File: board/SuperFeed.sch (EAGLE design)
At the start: 15 parts

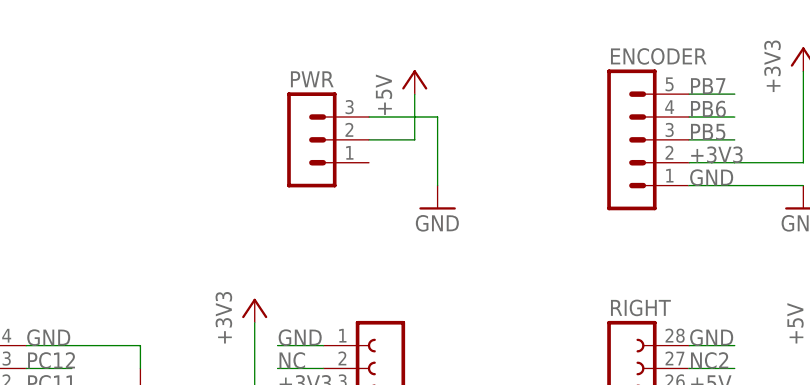
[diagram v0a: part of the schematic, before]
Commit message: Connect third pin to ground on power connector
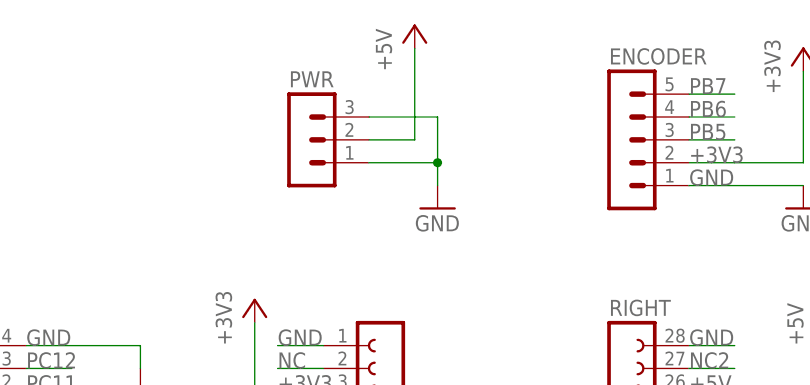
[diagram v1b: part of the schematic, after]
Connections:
- net GND: now also PWR.1
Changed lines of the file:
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@@
 <setting verticaltext="up"/>
 </settings>
-<grid distance="0.1" unitdist="inch" unit="inch" style="lines" multiple="1" display="yes" altdistance="0.01" altunitdist="inch" altunit="inch"/>
+<grid distance="0.1" unitdist="inch" unit="inch" style="lines" multiple="1" display="no" altdistance="0.01" altunitdist="inch" altunit="inch"/>
 <layers>
 <layer number="1" name="Top" color="4" fill="1" visible="no" active="no"/>
@@
 <instance part="PWR" gate="G$1" x="40.64" y="119.38"/>
 <instance part="SPINDLE" gate="1" x="88.9" y="-5.08"/>
-<instance part="P+4" gate="1" x="53.34" y="127"/>
+<instance part="P+4" gate="1" x="53.34" y="132.08"/>
 <instance part="GND4" gate="1" x="55.88" y="111.76"/>
 <instance part="GND5" gate="1" x="22.86" y="91.44"/>
@@
 <pinref part="PWR" gate="G$1" pin="3"/>
 <wire x1="48.26" y1="121.92" x2="55.88" y2="121.92" width="0.1524" layer="91"/>
-<wire x1="55.88" y1="121.92" x2="55.88" y2="114.3" width="0.1524" layer="91"/>
+<wire x1="55.88" y1="121.92" x2="55.88" y2="116.84" width="0.1524" layer="91"/>
 <pinref part="GND4" gate="1" pin="GND"/>
+<pinref part="PWR" gate="G$1" pin="1"/>
+<wire x1="55.88" y1="116.84" x2="55.88" y2="114.3" width="0.1524" layer="91"/>
+<wire x1="48.26" y1="116.84" x2="55.88" y2="116.84" width="0.1524" layer="91"/>
+<junction x="55.88" y="116.84"/>
 </segment>
 <segment>
@@
 <pinref part="P+4" gate="1" pin="+5V"/>
 <wire x1="48.26" y1="119.38" x2="53.34" y2="119.38" width="0.1524" layer="91"/>
-<wire x1="53.34" y1="119.38" x2="53.34" y2="124.46" width="0.1524" layer="91"/>
-</segment>
-<segment>
+<wire x1="53.34" y1="119.38" x2="53.34" y2="129.54" width="0.1524" layer="91"/>
+</segment>
+<segment>

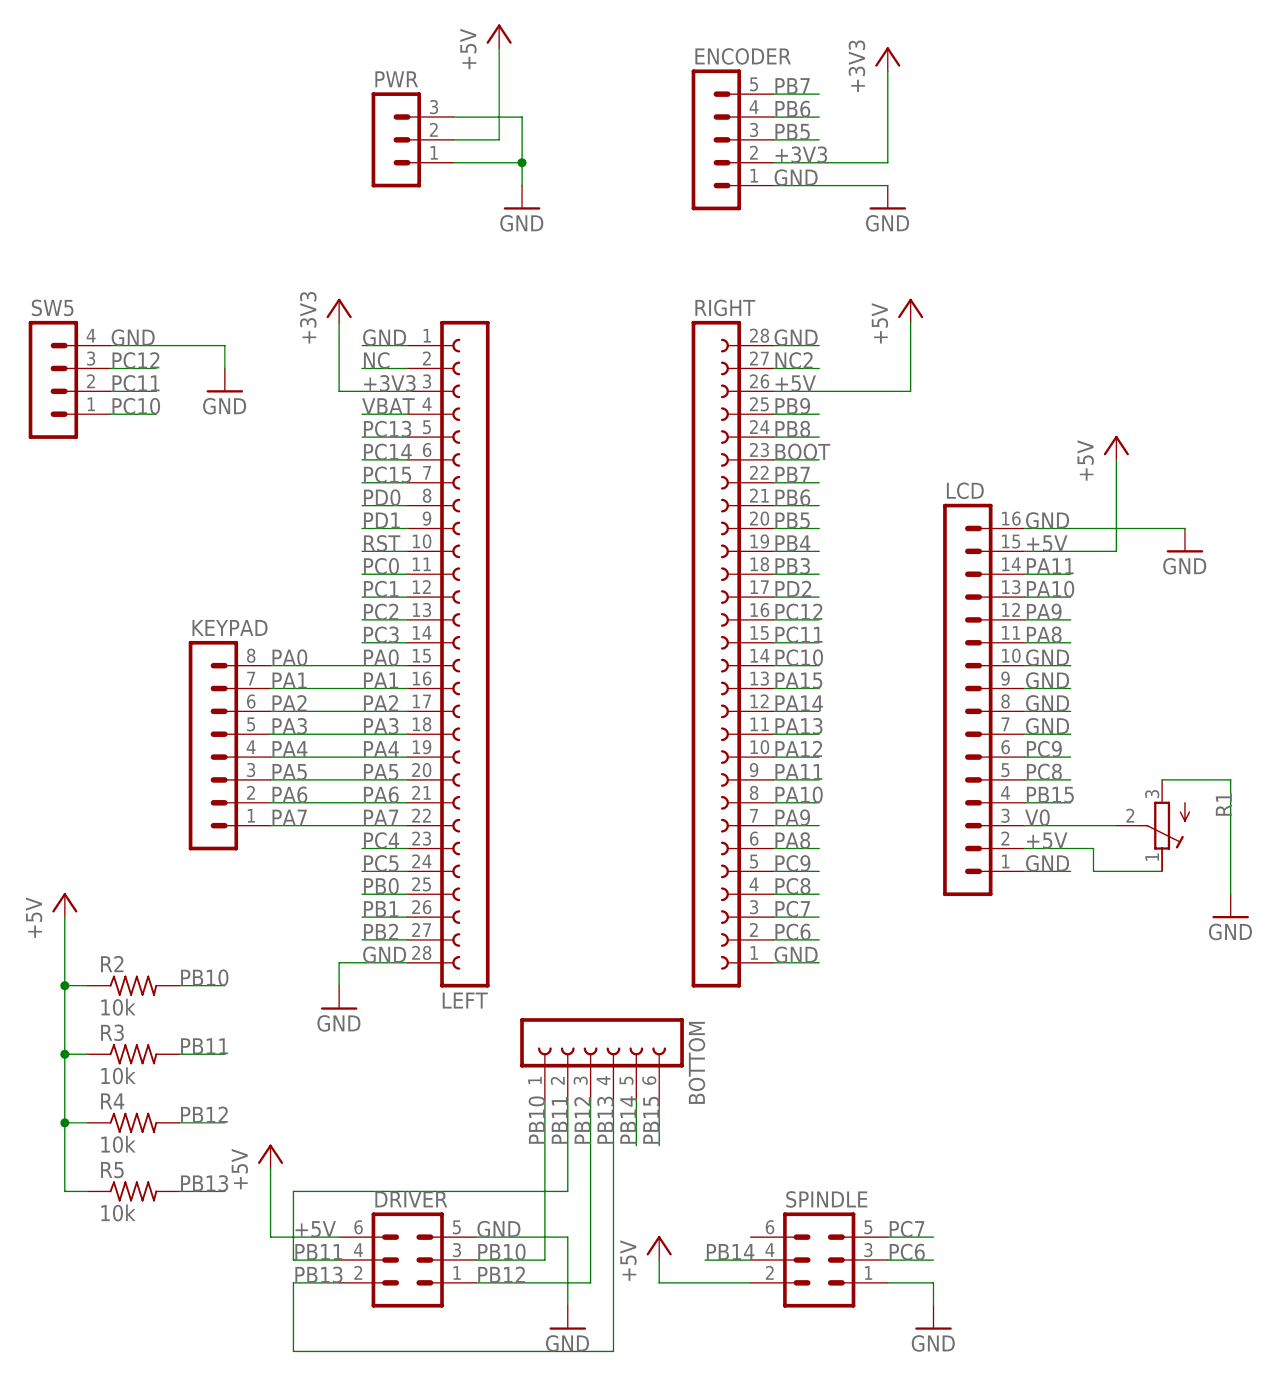
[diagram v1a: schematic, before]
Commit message: Adding extra buttons on board
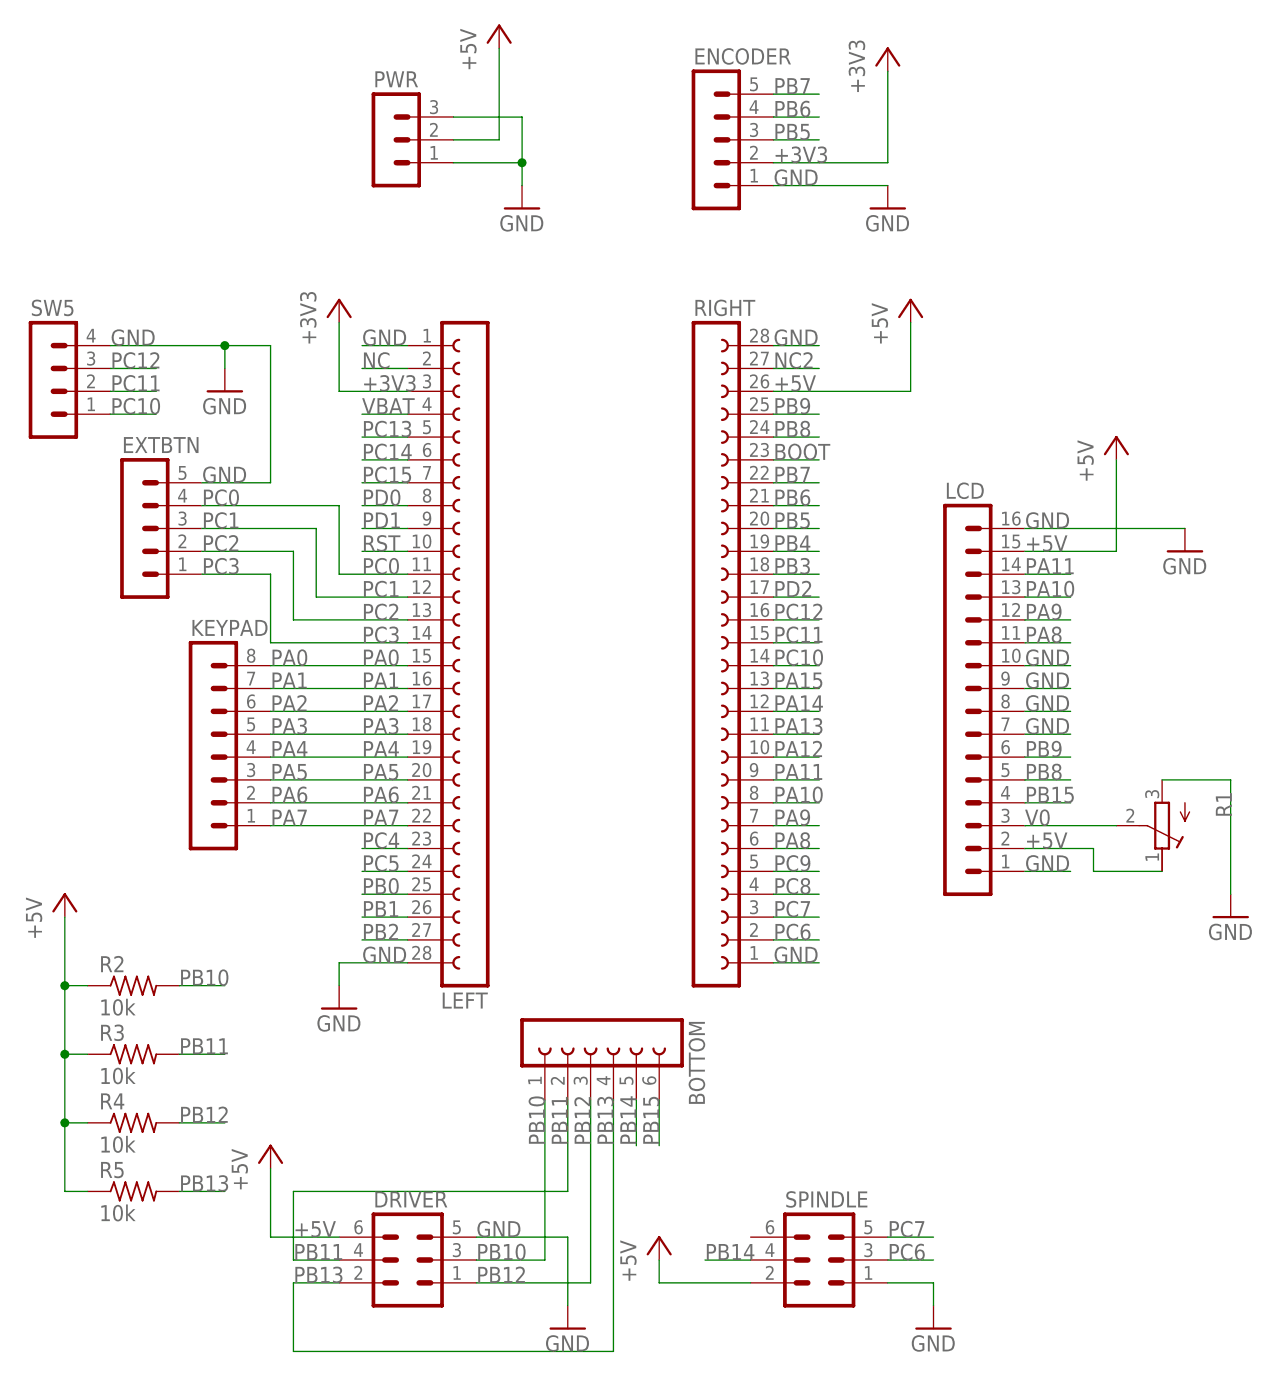
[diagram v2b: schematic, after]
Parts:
- added EXTBTN: (no value), SuperFeed:MA05-1W
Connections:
- net GND: now also EXTBTN.5
- net PB8: now also LCD.5
- net PB9: now also LCD.6
- net PC0: now also EXTBTN.4
- net PC1: now also EXTBTN.3
- net PC2: now also EXTBTN.2
- net PC3: now also EXTBTN.1
- net PC8: no longer LCD.5
- net PC9: no longer LCD.6
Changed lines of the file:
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@@
 <part name="R5" library="SuperFeed" deviceset="R-US_" device="0207/15" value="10k"/>
 <part name="P+5" library="SuperFeed" deviceset="+5V" device=""/>
+<part name="EXTBTN" library="SuperFeed" deviceset="MA05-1W" device=""/>
 </parts>
 <sheets>
@@
 <instance part="R5" gate="G$1" x="12.7" y="2.54"/>
 <instance part="P+5" gate="1" x="5.08" y="35.56"/>
+<instance part="EXTBTN" gate="G$1" x="12.7" y="76.2"/>
 </instances>
 <busses>
@@
 <wire x1="22.86" y1="96.52" x2="22.86" y2="93.98" width="0.1524" layer="91"/>
 <pinref part="GND5" gate="1" pin="GND"/>
+<pinref part="EXTBTN" gate="G$1" pin="5"/>
+<wire x1="20.32" y1="81.28" x2="27.94" y2="81.28" width="0.1524" layer="91"/>
+<wire x1="27.94" y1="81.28" x2="27.94" y2="96.52" width="0.1524" layer="91"/>
+<wire x1="27.94" y1="96.52" x2="22.86" y2="96.52" width="0.1524" layer="91"/>
+<junction x="22.86" y="96.52"/>
+<label x="20.32" y="81.28" size="1.778" layer="95"/>
 </segment>
 <segment>
@@
 <label x="83.82" y="88.9" size="1.778" layer="95"/>
 </segment>
+<segment>
+<pinref part="LCD" gate="G$1" pin="6"/>
+<wire x1="111.76" y1="50.8" x2="116.84" y2="50.8" width="0.1524" layer="91"/>
+<label x="111.76" y="50.8" size="1.778" layer="95"/>
+</segment>
 </net>
 <net name="PB8" class="0">
@@
 <label x="83.82" y="86.36" size="1.778" layer="95"/>
 </segment>
+<segment>
+<pinref part="LCD" gate="G$1" pin="5"/>
+<wire x1="111.76" y1="48.26" x2="116.84" y2="48.26" width="0.1524" layer="91"/>
+<label x="111.76" y="48.26" size="1.778" layer="95"/>
+</segment>
 </net>
 <net name="BOOT" class="0">
@@
 <label x="83.82" y="38.1" size="1.778" layer="95"/>
 </segment>
-<segment>
-<pinref part="LCD" gate="G$1" pin="6"/>
-<wire x1="111.76" y1="50.8" x2="116.84" y2="50.8" width="0.1524" layer="91"/>
-<label x="111.76" y="50.8" size="1.778" layer="95"/>
-</segment>
 </net>
 <net name="PC8" class="0">
@@
 <wire x1="88.9" y1="35.56" x2="83.82" y2="35.56" width="0.1524" layer="91"/>
 <label x="83.82" y="35.56" size="1.778" layer="95"/>
-</segment>
-<segment>
-<pinref part="LCD" gate="G$1" pin="5"/>
-<wire x1="111.76" y1="48.26" x2="116.84" y2="48.26" width="0.1524" layer="91"/>
-<label x="111.76" y="48.26" size="1.778" layer="95"/>
 </segment>
 </net>
@@
 <segment>
 <pinref part="LEFT" gate="G$1" pin="14"/>
-<wire x1="43.18" y1="63.5" x2="38.1" y2="63.5" width="0.1524" layer="91"/>
 <label x="38.1" y="63.5" size="1.778" layer="95"/>
+<wire x1="43.18" y1="63.5" x2="27.94" y2="63.5" width="0.1524" layer="91"/>
+<wire x1="27.94" y1="63.5" x2="27.94" y2="71.12" width="0.1524" layer="91"/>
+<pinref part="EXTBTN" gate="G$1" pin="1"/>
+<wire x1="27.94" y1="71.12" x2="20.32" y2="71.12" width="0.1524" layer="91"/>
+<label x="20.32" y="71.12" size="1.778" layer="95"/>
 </segment>
 </net>
@@
 <segment>
 <pinref part="LEFT" gate="G$1" pin="13"/>
-<wire x1="43.18" y1="66.04" x2="38.1" y2="66.04" width="0.1524" layer="91"/>
 <label x="38.1" y="66.04" size="1.778" layer="95"/>
+<wire x1="43.18" y1="66.04" x2="30.48" y2="66.04" width="0.1524" layer="91"/>
+<wire x1="30.48" y1="66.04" x2="30.48" y2="73.66" width="0.1524" layer="91"/>
+<pinref part="EXTBTN" gate="G$1" pin="2"/>
+<wire x1="30.48" y1="73.66" x2="20.32" y2="73.66" width="0.1524" layer="91"/>
+<label x="20.32" y="73.66" size="1.778" layer="95"/>
 </segment>
 </net>
@@
 <segment>
 <pinref part="LEFT" gate="G$1" pin="12"/>
-<wire x1="43.18" y1="68.58" x2="38.1" y2="68.58" width="0.1524" layer="91"/>
 <label x="38.1" y="68.58" size="1.778" layer="95"/>
+<wire x1="43.18" y1="68.58" x2="33.02" y2="68.58" width="0.1524" layer="91"/>
+<wire x1="33.02" y1="68.58" x2="33.02" y2="76.2" width="0.1524" layer="91"/>
+<pinref part="EXTBTN" gate="G$1" pin="3"/>
+<wire x1="33.02" y1="76.2" x2="20.32" y2="76.2" width="0.1524" layer="91"/>
+<label x="20.32" y="76.2" size="1.778" layer="95"/>
 </segment>
 </net>
@@
 <segment>
 <pinref part="LEFT" gate="G$1" pin="11"/>
-<wire x1="43.18" y1="71.12" x2="38.1" y2="71.12" width="0.1524" layer="91"/>
+<wire x1="43.18" y1="71.12" x2="35.56" y2="71.12" width="0.1524" layer="91"/>
 <label x="38.1" y="71.12" size="1.778" layer="95"/>
-</segment>
-</net>
+<wire x1="35.56" y1="71.12" x2="35.56" y2="78.74" width="0.1524" layer="91"/>
+<pinref part="EXTBTN" gate="G$1" pin="4"/>
+<wire x1="35.56" y1="78.74" x2="20.32" y2="78.74" width="0.1524" layer="91"/>
+<label x="20.32" y="78.74" size="1.778" layer="95"/>
+</segment>
+</net>
